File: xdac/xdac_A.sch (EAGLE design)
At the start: 3 parts, among them J1 LIWE_40_PIN, U1 STA311B

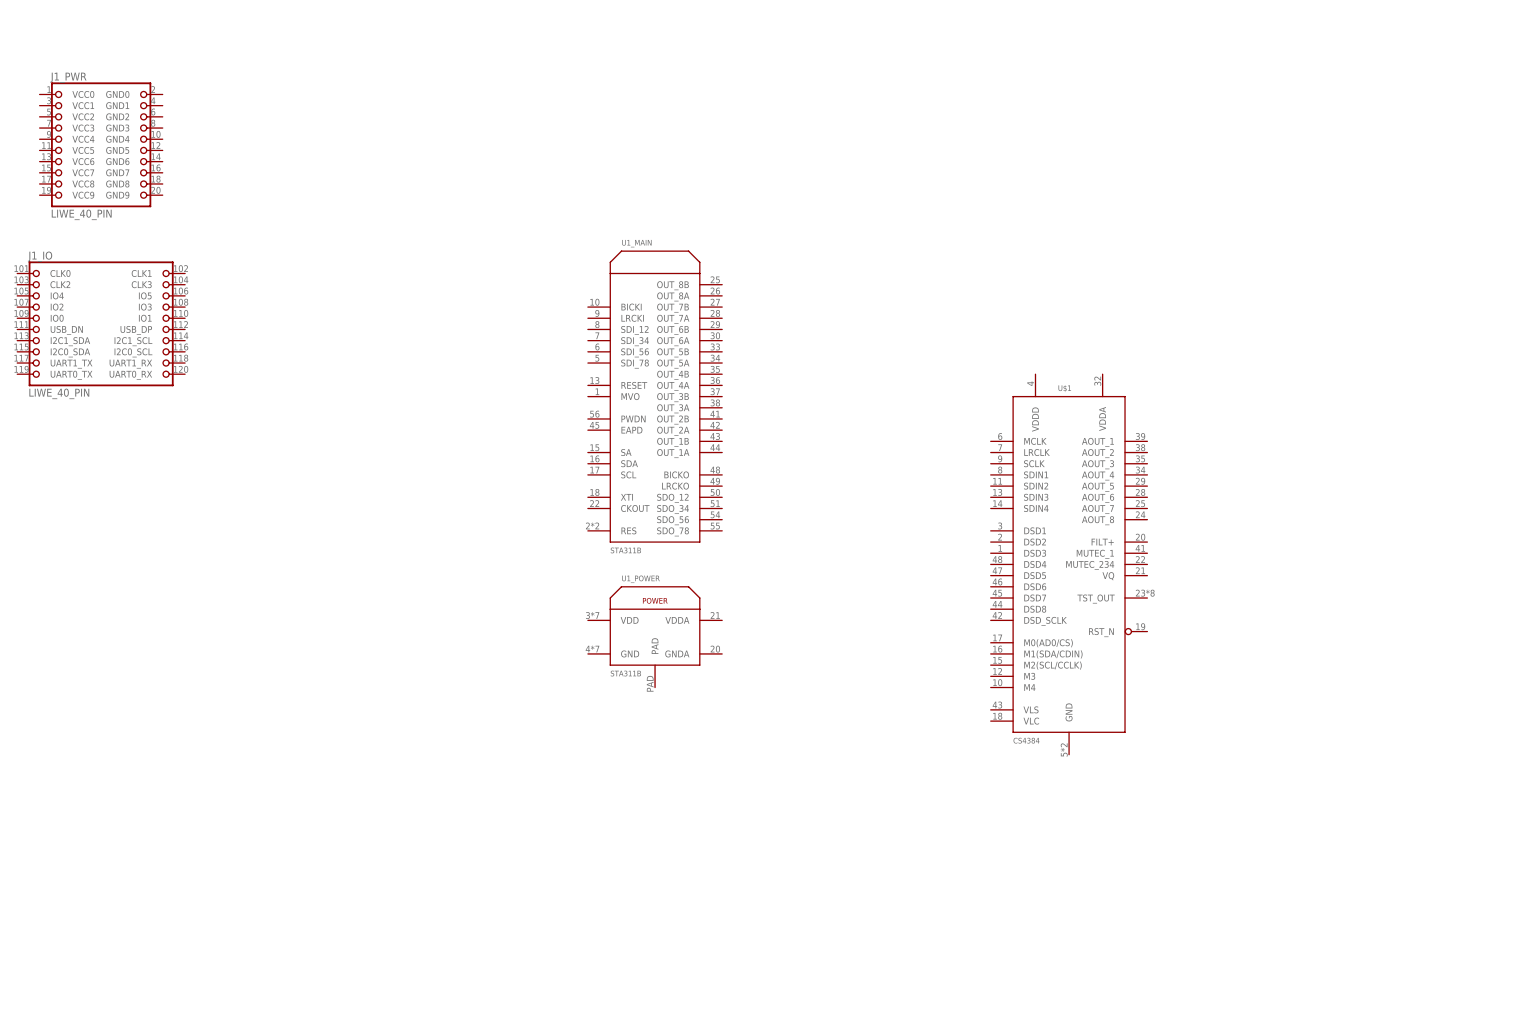
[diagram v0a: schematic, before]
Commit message: xdac: VIP schematic in progress.
Signed-off-by: malo <pavol.malosek@gmail.com>
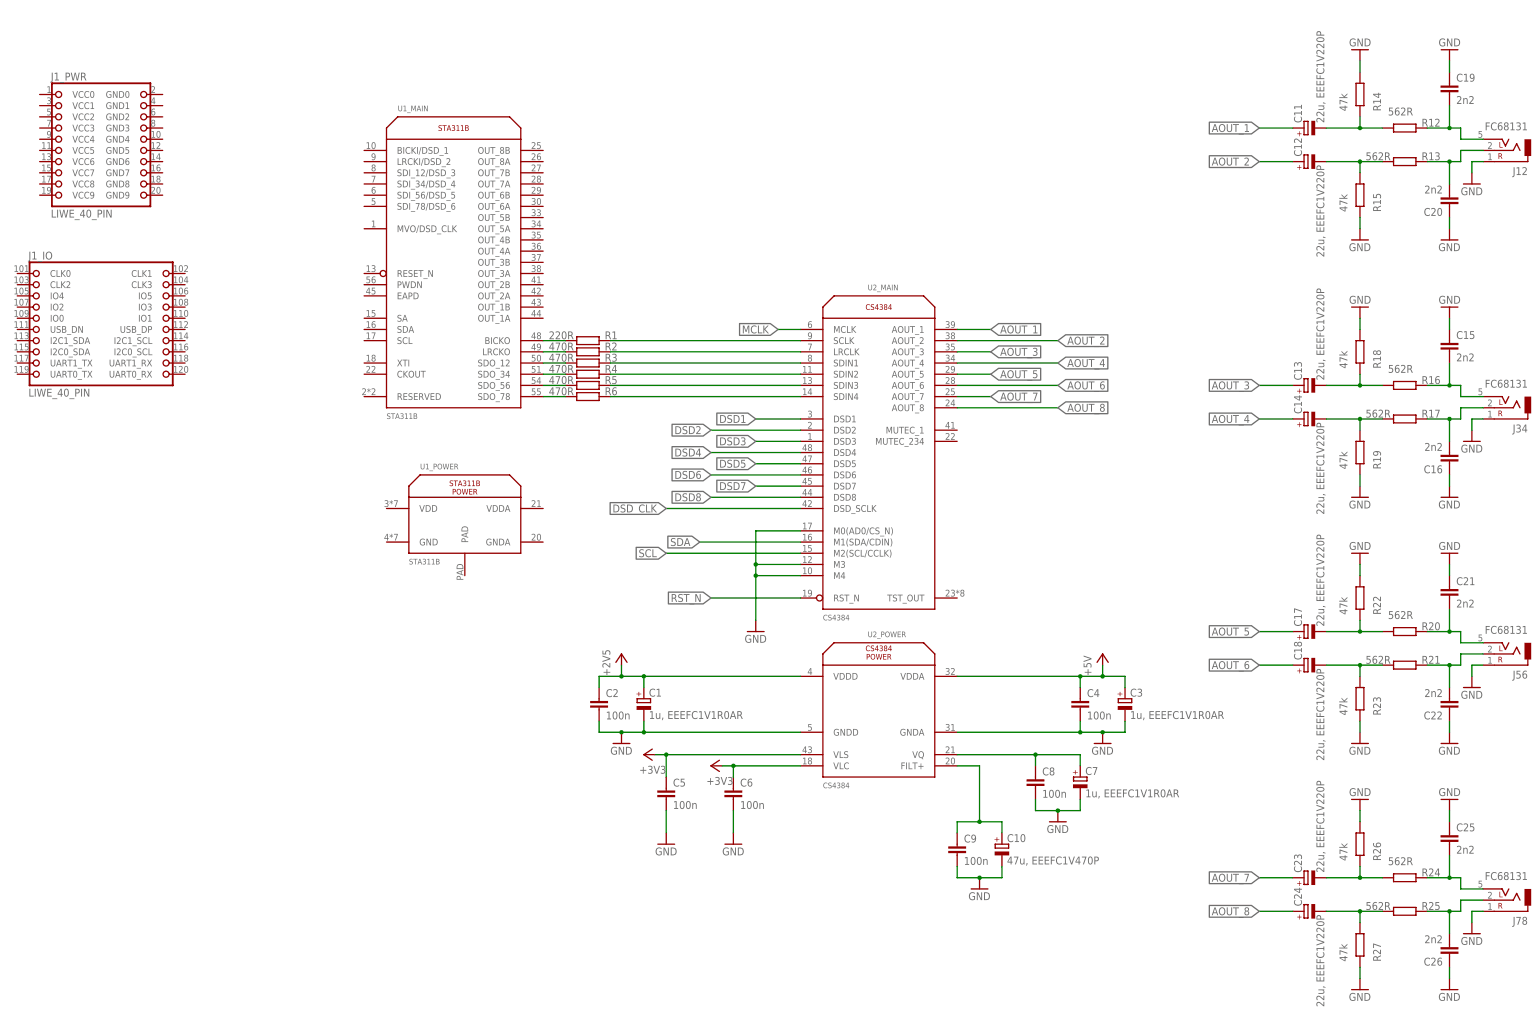
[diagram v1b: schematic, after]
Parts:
- removed U$1: CS4384, 25cmsquare:CS4384
- added C1, C3, C7: 1u, EEEFC1V1R0AR, 25cmsquare:C-POL_B
- added C10: 47u, EEEFC1V470P, 25cmsquare:C-POL_E
- added C11, C12, C13, C14, C17, C18, C23, C24: 22u, EEEFC1V220P, 25cmsquare:C-POL_D
- added C15, C16, C19, C20, C21, C22, C25, C26: 2n2, rcl:C-EUC0603K
- added C2, C4, C5, C6, C8, C9: 100n, rcl:C-EUC0603K
- added J12, J34, J56, J78: FC68131, 25cmsquare:JACK_3.5_3P
- added R1: 220R, rcl:R-EU_R0603
- added R12, R13, R16, R17, R20, R21, R24, R25: 562R, rcl:R-EU_R0603
- added R14, R15, R18, R19, R22, R23, R26, R27: 47k, rcl:R-EU_R0603
- added R2, R3, R4, R5, R6: 470R, rcl:R-EU_R0603
- added U2: CS4384, 25cmsquare:CS4384
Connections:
- new net +2V5: C1.+, C2.1, U2_POWER.VDDD
- new net +3V3: C5.1, C6.1, U2_POWER.VLC, U2_POWER.VLS
- new net +5V: C3.+, C4.1, U2_POWER.VDDA
- new net AOUT_1: C11.+, U2_MAIN.AOUT_1
- new net AOUT_2: C12.+, U2_MAIN.AOUT_2
- new net AOUT_3: C13.+, U2_MAIN.AOUT_3
- new net AOUT_4: C14.+, U2_MAIN.AOUT_4
- new net AOUT_5: C17.+, U2_MAIN.AOUT_5
- new net AOUT_6: C18.+, U2_MAIN.AOUT_6
- new net AOUT_7: C23.+, U2_MAIN.AOUT_7
- new net AOUT_8: C24.+, U2_MAIN.AOUT_8
- new net DSD1: U2_MAIN.DSD1
- new net DSD2: U2_MAIN.DSD2
- new net DSD3: U2_MAIN.DSD3
- new net DSD4: U2_MAIN.DSD4
- new net DSD5: U2_MAIN.DSD5
- new net DSD6: U2_MAIN.DSD6
- new net DSD7: U2_MAIN.DSD7
- new net DSD8: U2_MAIN.DSD8
- new net DSD_CLK: U2_MAIN.DSD_SCLK
- new net GND: C1.-, C10.-, C15.1, C16.1, C19.1, C2.2, C20.1, C21.1, C22.1, C25.1, C26.1, C3.-, C4.2, C5.2, C6.2, C7.-, C8.2, C9.2, J12.1, J34.1, J56.1, J78.1, R14.2, R15.1, R18.2, R19.1, R22.2, R23.1, R26.2, R27.1, U2_MAIN.M0(AD0/CS_N), U2_MAIN.M3, U2_MAIN.M4, U2_POWER.GNDA, U2_POWER.GNDD
- new net MCLK: U2_MAIN.MCLK
- new net N$1: R1.1, U1_MAIN.BICKO
- new net N$10: R4.2, U2_MAIN.SDIN2
- new net N$11: R5.2, U2_MAIN.SDIN3
- new net N$12: R6.2, U2_MAIN.SDIN4
- new net N$13: C19.2, J12.3, R12.2
- new net N$14: C20.2, J12.2, R13.2
- new net N$15: C11.-, R12.1, R14.1
- new net N$16: C12.-, R13.1, R15.2
- new net N$2: R2.1, U1_MAIN.LRCKO
- new net N$23: C10.+, C9.1, U2_POWER.FILT+
- new net N$25: C16.2, J34.2, R17.2
- new net N$26: C7.+, C8.1, U2_POWER.VQ
- new net N$27: C13.-, R16.1, R18.1
- new net N$28: C14.-, R17.1, R19.2
- new net N$29: C15.2, J34.3, R16.2
- new net N$3: R3.1, U1_MAIN.SDO_12
- new net N$32: C22.2, J56.2, R21.2
- new net N$33: C17.-, R20.1, R22.1
- new net N$34: C18.-, R21.1, R23.2
- new net N$35: C21.2, J56.3, R20.2
- new net N$38: C26.2, J78.2, R25.2
- new net N$39: C23.-, R24.1, R26.1
- new net N$4: R4.1, U1_MAIN.SDO_34
- new net N$40: C24.-, R25.1, R27.2
- new net N$41: C25.2, J78.3, R24.2
- new net N$5: R5.1, U1_MAIN.SDO_56
- new net N$6: R6.1, U1_MAIN.SDO_78
- new net N$7: R1.2, U2_MAIN.SCLK
- new net N$8: R2.2, U2_MAIN.LRCLK
- new net N$9: R3.2, U2_MAIN.SDIN1
- new net RST_N: U2_MAIN.RST_N
- new net SCL: U2_MAIN.M2(SCL/CCLK)
- new net SDA: U2_MAIN.M1(SDA/CDIN)
